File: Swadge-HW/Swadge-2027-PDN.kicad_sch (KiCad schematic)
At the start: 3 parts, among them SW9 SW_SPDT_1825232-1

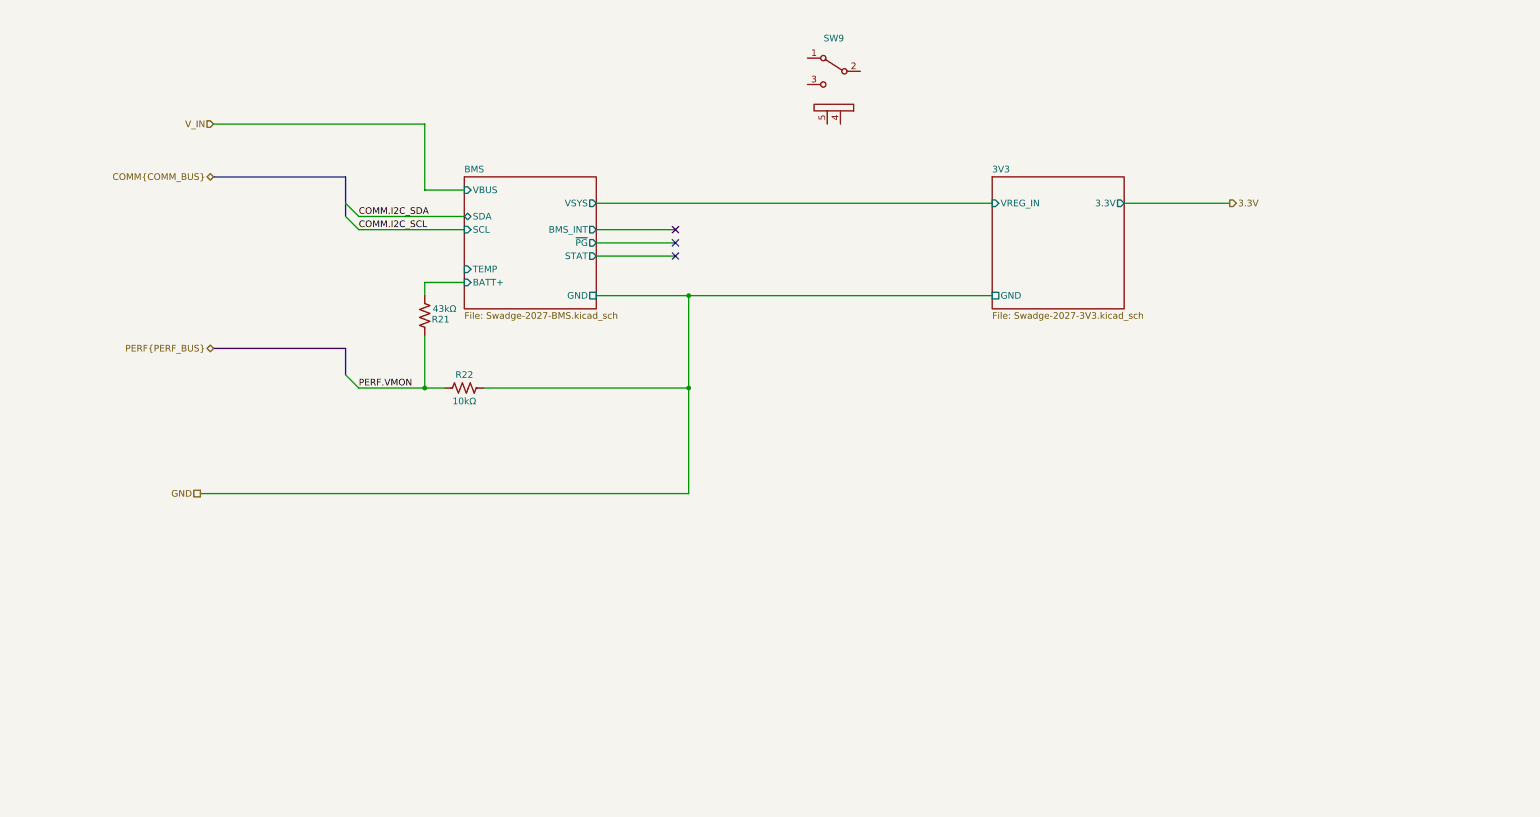
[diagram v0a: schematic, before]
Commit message: Bus Renames
Since we really don't have that many signals I just ditched the bus prefixes and Alias'd them directly.
Added a bus for the interupt and status signals even if they are never used.
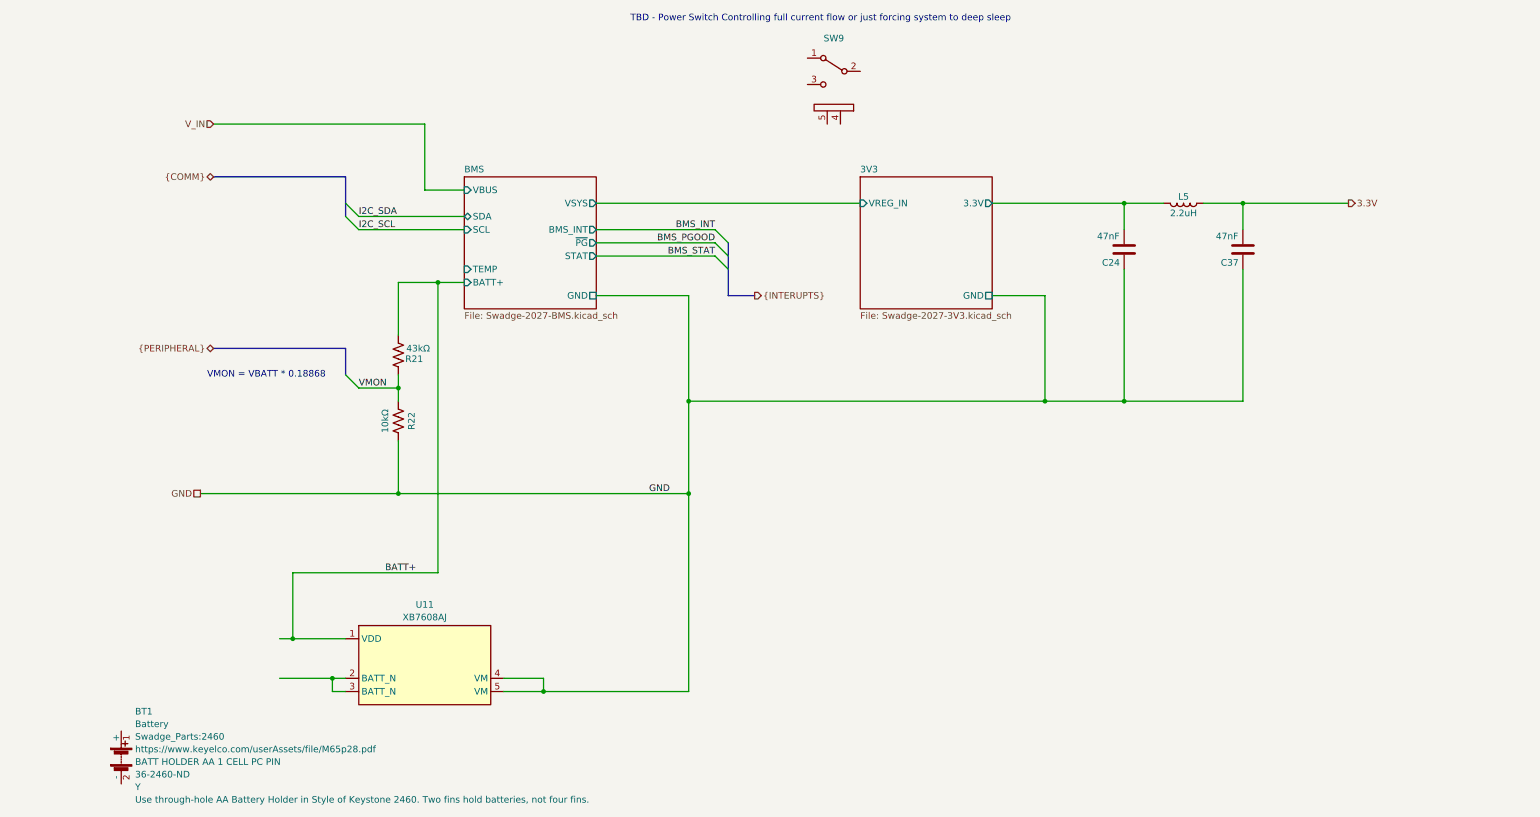
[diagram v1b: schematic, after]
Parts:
- added BT1: Battery, Swadge_Parts:2460, symbol Swadge_Parts:Battery
- added C24, C37: 47nF, Capacitor_SMD:C_0603_1608Metric, symbol Swadge_Parts:C
- added L5: 2.2uH, Inductor_SMD:L_1008_2520Metric, symbol Swadge_Parts:L
- added U11: XB7608AJ, sao:CPC-5_2.6mmx4mm_P0.53mm, symbol sao:XB7608AJ
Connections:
- net 3.3V: now also C37.1, L5.1
- net GND: now also C24.2, C37.2, U11.4 (VM), U11.5 (VM)
- net BMS/BATT+ renamed BATT+
- net BATT+: now also U11.1 (VDD)
- net PERF.VMON renamed VMON
- new net: U11.2 (BATT_N), U11.3 (BATT_N)
- new net 3V3/3.3V: C24.1, L5.2
- no-connect marks 3 -> 0
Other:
- note added: "TBD - Power Switch Controlling full current flow or just forcing system to deep sleep"
- note added: "VMON = VBATT * 0.18868"
- moved on the sheet: R21, R22

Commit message: Annotations
Updated Annotations with zonal numbering
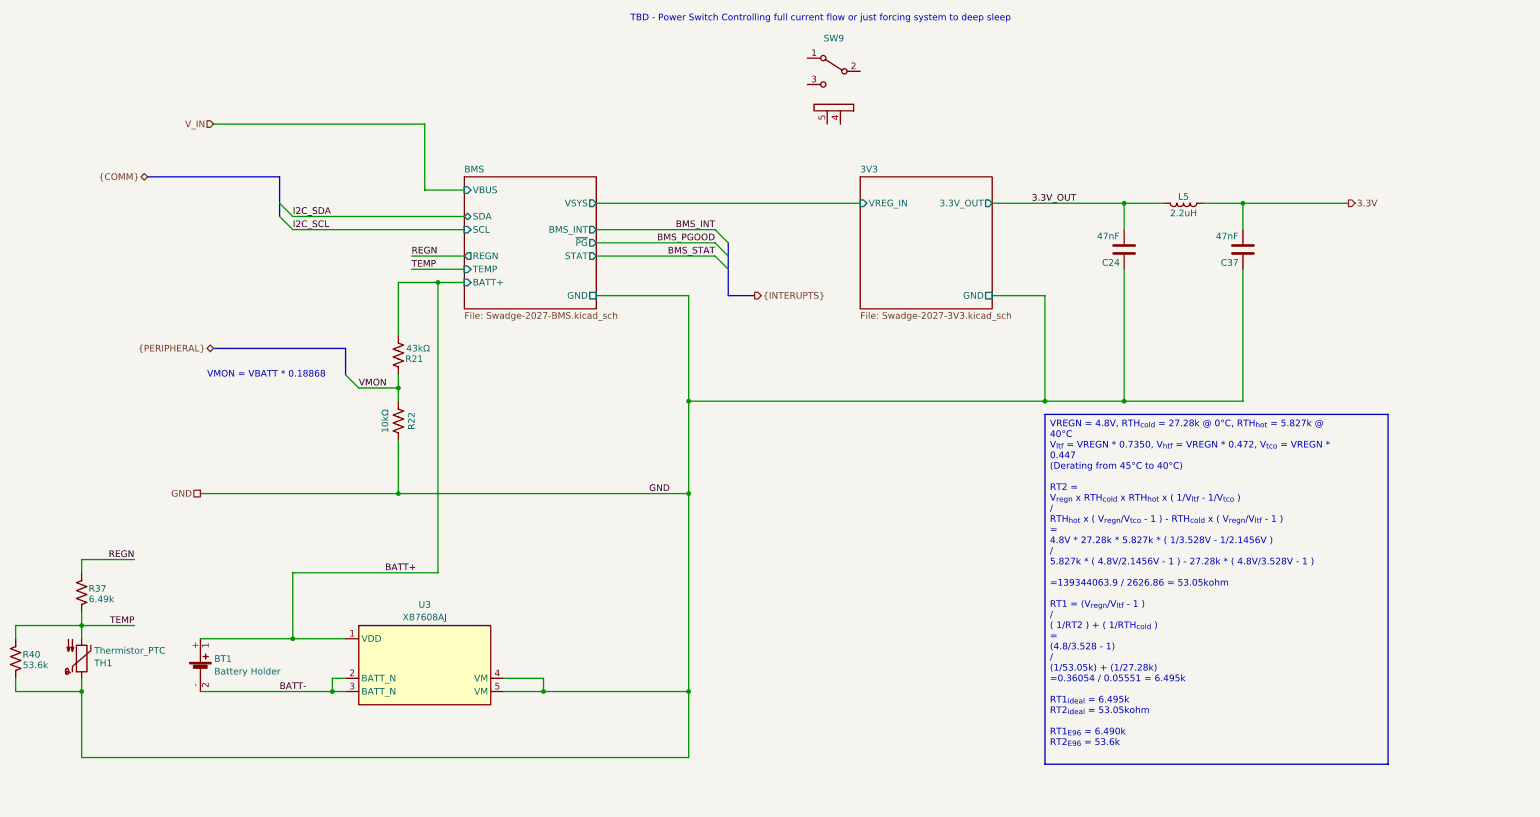
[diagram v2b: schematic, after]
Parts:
- added R37: 6.49k, Resistor_SMD:R_0603_1608Metric, symbol Swadge_Parts:R_US
- added R40: 53.6k, Resistor_SMD:R_0603_1608Metric, symbol Swadge_Parts:R_US
- added TH1: Thermistor_PTC, symbol Device:Thermistor_PTC
- BT1: value Battery -> Battery Holder; footprint Swadge_Parts:2460 -> Swadge_Parts:BH-18650-Bxxx002; symbol Swadge_Parts:Battery -> Swadge_Parts:1x18650_Battery_Holder; Cost @ 2.5k (none) -> 0.9186; Digikey 36-2460-ND -> 36-1042P-ND; LCSC (none) -> C2988620; Notes Use through-hole AA Battery Holder in Style of Keystone 246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 -> (none)
- renumbered U11 to U3
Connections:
- net BATT+: now also BT1.1 (+)
- net GND: now also R40.2, TH1.1
- net BATT-: now reaches U3.2 (BATT_N), U3.3 (BATT_N)
- net BATT-: now also BT1.2 (-)
- net 3V3/3.3V renamed 3.3V_OUT
- new net REGN: R37.1
- new net TEMP: R37.2, R40.1, TH1.2
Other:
- sheet 3V3 ports: added 3.3V_OUT; removed 3.3V
- sheet BMS ports: added REGN; removed none

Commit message: Cleanup
Renamed some components
Added in some net directives
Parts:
- R37: Cost @ 2.5k 0.001 -> 0.0016; LCSC C25973 -> C23088
- R40: Cost @ 2.5k 0.0018 -> 0.0044; Cost100 0.22 -> 0.0049; LCSC 25967 -> C23074
- TH1: value Thermistor_PTC -> Thermistor_NTC; footprint (none) -> Swadge_Parts:R_0603_1608Metric; symbol Device:Thermistor_PTC -> Device:Thermistor_NTC; Cost @ 2.5k (none) -> 0.0129; LCSC (none) -> C41417292
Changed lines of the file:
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@@
 			)
 		)
-		(property "Cost100" "0.22"
+		(property "Cost100" "0.0049"
 			(at 15.24 143.51 0)
 			(hide yes)
@@
 			)
 		)
-		(property "LCSC" "25967"
+		(property "LCSC" "C23074"
 			(at 15.24 143.51 0)
 			(hide yes)
@@
 			)
 		)
-		(property "Cost @ 2.5k" "0.0018"
+		(property "Cost @ 2.5k" "0.0044"
 			(at 15.24 143.51 0)
 			(hide yes)
@@
 			)
 		)
-		(property "LCSC" "C25973"
+		(property "LCSC" "C23088"
 			(at 27.94 130.81 0)
 			(hide yes)
@@
 			)
 		)
-		(property "Cost @ 2.5k" "0.001"
+		(property "Cost @ 2.5k" "0.0016"
 			(at 27.94 130.81 0)
 			(hide yes)
@@
 	)
 	(symbol
-		(lib_id "Device:Thermistor_PTC")
+		(lib_id "Device:Thermistor_NTC")
 		(at 27.94 143.51 0)
 		(mirror x)
@@
 			)
 		)
-		(property "Value" "Thermistor_PTC"
+		(property "Value" "Thermistor_NTC"
 			(at 30.353 141.9804 0)
 			(show_name no)
@@
 			)
 		)
-		(property "Footprint" ""
+		(property "Footprint" "Swadge_Parts:R_0603_1608Metric"
 			(at 29.21 138.43 0)
 			(hide yes)
@@
 			)
 		)
-		(property "Datasheet" ""
+		(property "Datasheet" "https://www.lcsc.com/datasheet/C41417292.pdf"
 			(at 27.94 143.51 0)
 			(hide yes)
@@
 			)
 		)
-		(property "Description" "Temperature dependent resistor, positive temperature coefficient"
+		(property "Description" "Temperature dependent resistor, negative temperature coefficient"
 			(at 27.94 143.51 0)
 			(hide yes)
+			(show_name no)
+			(do_not_autoplace no)
+			(effects
+				(font
+					(size 1.27 1.27)
+				)
+			)
+		)
+		(property "LCSC" "C41417292"
+			(at 27.94 143.51 0)
+			(hide yes)
+			(show_name no)
+			(do_not_autoplace no)
+			(effects
+				(font
+					(size 1.27 1.27)
+				)
+			)
+		)
+		(property "Cost @ 2.5k" "0.0129"
+			(at 27.94 143.51 0)
+			(hide yes)

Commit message: Starting PCB
Very Rough Initial Layout
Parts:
- U3: footprint sao:CPC-5_2.6mmx4mm_P0.53mm -> Swadge_Parts:CPC-5_2.6mmx4mm_P0.53mm
- renumbered C24 to C54, C37 to C55, L5 to L52, R21 to R31, R22 to R32, R37 to R33, R40 to R34
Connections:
- no-connect marks 0 -> 5
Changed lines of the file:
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@@
 		(color 0 0 0 0)
+	)
+	(no_connect
+		(at 173.99 40.64)
+	)
+	(no_connect
+		(at 167.64 27.94)
+	)
+	(no_connect
+		(at 171.45 40.64)
+	)
+	(no_connect
+		(at 177.8 30.48)
+	)
+	(no_connect
+		(at 167.64 33.02)
 	)
 	(bus_entry
@@
 			)
 		)
-		(property "Footprint" "sao:CPC-5_2.6mmx4mm_P0.53mm"
+		(property "Footprint" "Swadge_Parts:CPC-5_2.6mmx4mm_P0.53mm"
 			(at 93.98 144.78 0)
 			(hide yes)
@@
 		(in_pos_files yes)
 		(dnp no)
-		(property "Reference" "R21"
+		(property "Reference" "R31"
 			(at 91.948 85.852 0)
 			(show_name no)
@@
 			(project "Swadge-HW"
 				(path "/770c762f-3a30-4864-b7da-de353459cdd6/83e4033f-0c15-4157-a463-52f03cd15801"
-					(reference "R21")
+					(reference "R31")
 					(unit 1)
 				)
@@
 		(in_pos_files yes)
 		(dnp no)
-		(property "Reference" "R40"
+		(property "Reference" "R34"
 			(at 18.288 142.748 0)
 			(show_name no)
@@
 			(project "Swadge-HW"
 				(path "/770c762f-3a30-4864-b7da-de353459cdd6/83e4033f-0c15-4157-a463-52f03cd15801"
-					(reference "R40")
+					(reference "R34")
 					(unit 1)
 				)
@@
 		(in_pos_files yes)
 		(dnp no)
-		(property "Reference" "L5"
+		(property "Reference" "L52"
 			(at 240.03 54.61 90)
 			(show_name no)
@@
 			(project "Swadge-HW"
 				(path "/770c762f-3a30-4864-b7da-de353459cdd6/83e4033f-0c15-4157-a463-52f03cd15801"
-					(reference "L5")
+					(reference "L52")
 					(unit 1)
 				)
@@
 		(in_pos_files yes)
 		(dnp no)
-		(property "Reference" "C24"
+		(property "Reference" "C54"
 			(at 226.06 67.31 0)
 			(show_name no)
@@
 			(project "Swadge-HW"
 				(path "/770c762f-3a30-4864-b7da-de353459cdd6/83e4033f-0c15-4157-a463-52f03cd15801"
-					(reference "C24")
+					(reference "C54")
 					(unit 1)
 				)
@@
 		(in_pos_files yes)
 		(dnp no)
-		(property "Reference" "C37"
+		(property "Reference" "C55"
 			(at 248.92 67.31 0)
 			(show_name no)
@@
 			(project "Swadge-HW"
 				(path "/770c762f-3a30-4864-b7da-de353459cdd6/83e4033f-0c15-4157-a463-52f03cd15801"
-					(reference "C37")
+					(reference "C55")
 					(unit 1)
 				)
@@
 		(in_pos_files yes)
 		(dnp no)
-		(property "Reference" "R37"
+		(property "Reference" "R33"
 			(at 30.988 130.048 0)
 			(show_name no)
@@
 			(project "Swadge-HW"
 				(path "/770c762f-3a30-4864-b7da-de353459cdd6/83e4033f-0c15-4157-a463-52f03cd15801"
-					(reference "R37")
+					(reference "R33")
 					(unit 1)
 				)
@@
 		(in_pos_files yes)
 		(dnp no)
-		(property "Reference" "R22"
+		(property "Reference" "R32"
 			(at 91.44 97.79 90)
 			(show_name no)
@@
 			(project "Swadge-HW"
 				(path "/770c762f-3a30-4864-b7da-de353459cdd6/83e4033f-0c15-4157-a463-52f03cd15801"
-					(reference "R22")
+					(reference "R32")
 					(unit 1)
 				)
@@
 			(project "Swadge-HW"
 				(path "/770c762f-3a30-4864-b7da-de353459cdd6/83e4033f-0c15-4157-a463-52f03cd15801"
-					(page "2")
-				)
-			)
+					(page "5")
+				)
+			)

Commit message: major routing changes
Routed SPI
Started Test Routing Touch Inputs
Rough routing for LCD Power
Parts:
- C54, C55: Cost @ 2.5k (none) -> 0.0071
- R32: Cost @ 2.5k 0.0007 -> 0.0037; LCSC C25804 -> C2906982
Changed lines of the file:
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@@
+			)
+		)
+		(property "Cost @ 2.5k" "0.0071"
+			(at 228.6 64.77 0)
+			(hide yes)
+			(show_name no)
+			(do_not_autoplace no)
+			(effects
+				(font
+					(size 1.27 1.27)
+				)
 			)
 		)
@@
 			)
 		)
+		(property "Cost @ 2.5k" "0.0071"
+			(at 251.46 64.77 0)
+			(hide yes)
+			(show_name no)
+			(do_not_autoplace no)
+			(effects
+				(font
+					(size 1.27 1.27)
+				)
+			)
+		)
 		(pin "1"
 		)
@@
 			)
 		)
-		(property "LCSC" "C25804"
+		(property "LCSC" "C2906982"
 			(at 88.9 97.79 0)
 			(hide yes)
@@
 			)
 		)
-		(property "Cost @ 2.5k" "0.0007"
+		(property "Cost @ 2.5k" "0.0037"
 			(at 88.9 97.79 0)
 			(hide yes)

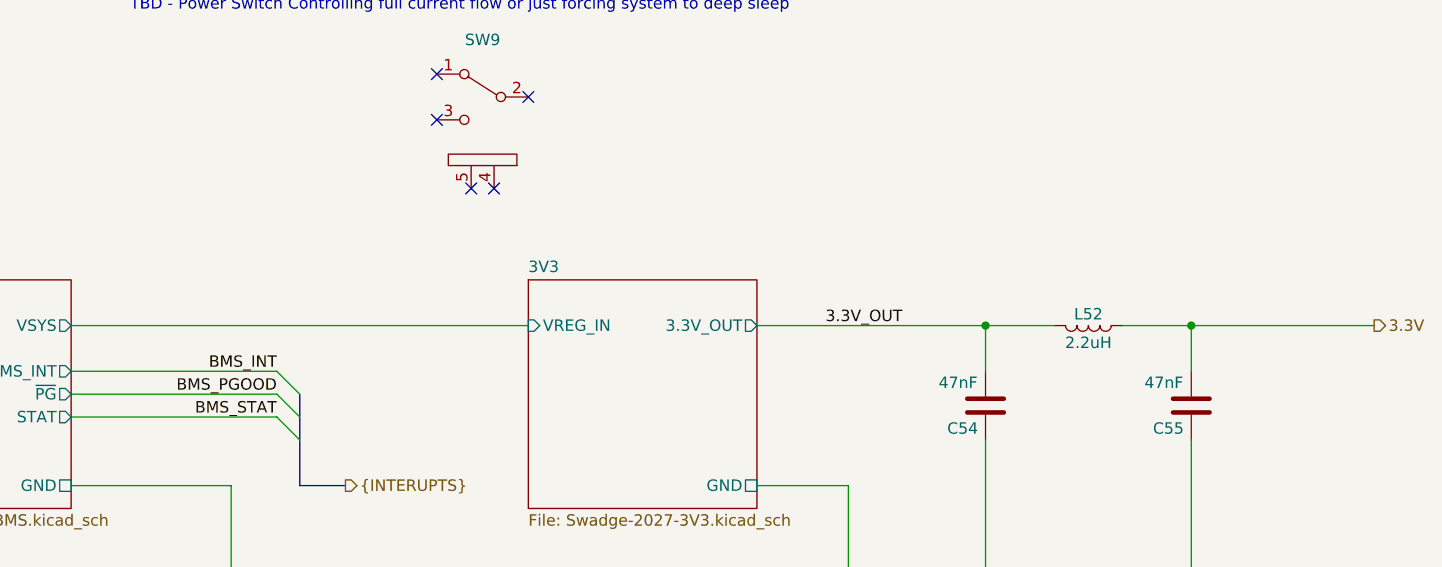
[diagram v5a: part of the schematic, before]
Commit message: Layout Changes
Moved USB 10deg around perimeter to get it closer to the ESP32 and the left thigh.
Substantially compressed BMS and 3.3V layout
Started Routing the Touch Inputs
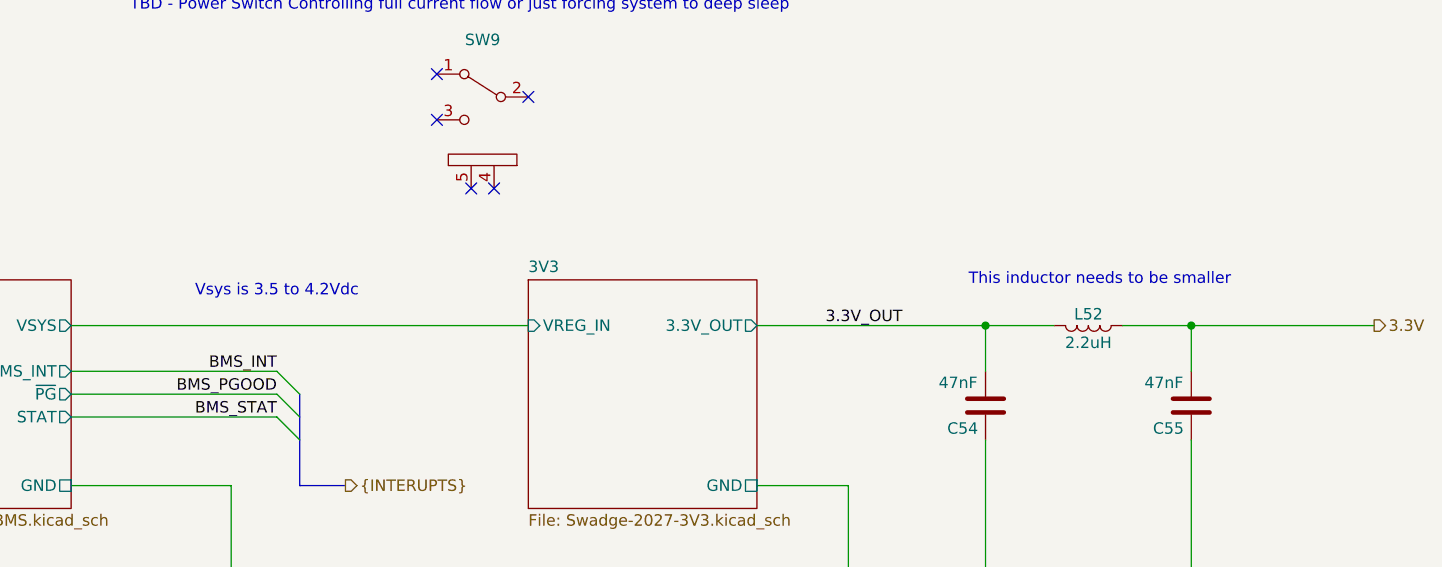
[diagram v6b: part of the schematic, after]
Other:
- note added: "This inductor needs to be smaller"
- note added: "Vsys is 3.5 to 4.2Vdc"
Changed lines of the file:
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@@
+		)
+	)
+	(text "This inductor needs to be smaller"
+		(exclude_from_sim no)
+		(at 241.3 50.8 0)
+		(effects
+			(font
+				(size 1.27 1.27)
+			)
+		)
+	)
+	(text "Vsys is 3.5 to 4.2Vdc"
+		(exclude_from_sim no)
+		(at 149.86 52.07 0)
+		(effects
+			(font
+				(size 1.27 1.27)
+			)
 		)
 	)
